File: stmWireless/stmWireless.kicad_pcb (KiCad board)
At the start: 4 copper layers, 49 parts, among them IC1 BALFLB-WL-02D3, J1 SWD, J2 CORTEX_DEBUG, J3 Power, J5 i2c3 header, U1 STM32WLE5CBU6, U2 AP63203WU, U3 BGS12WN6E6327, Y1 Crystal_32MHz, Y2 Crystal_32.768kHz

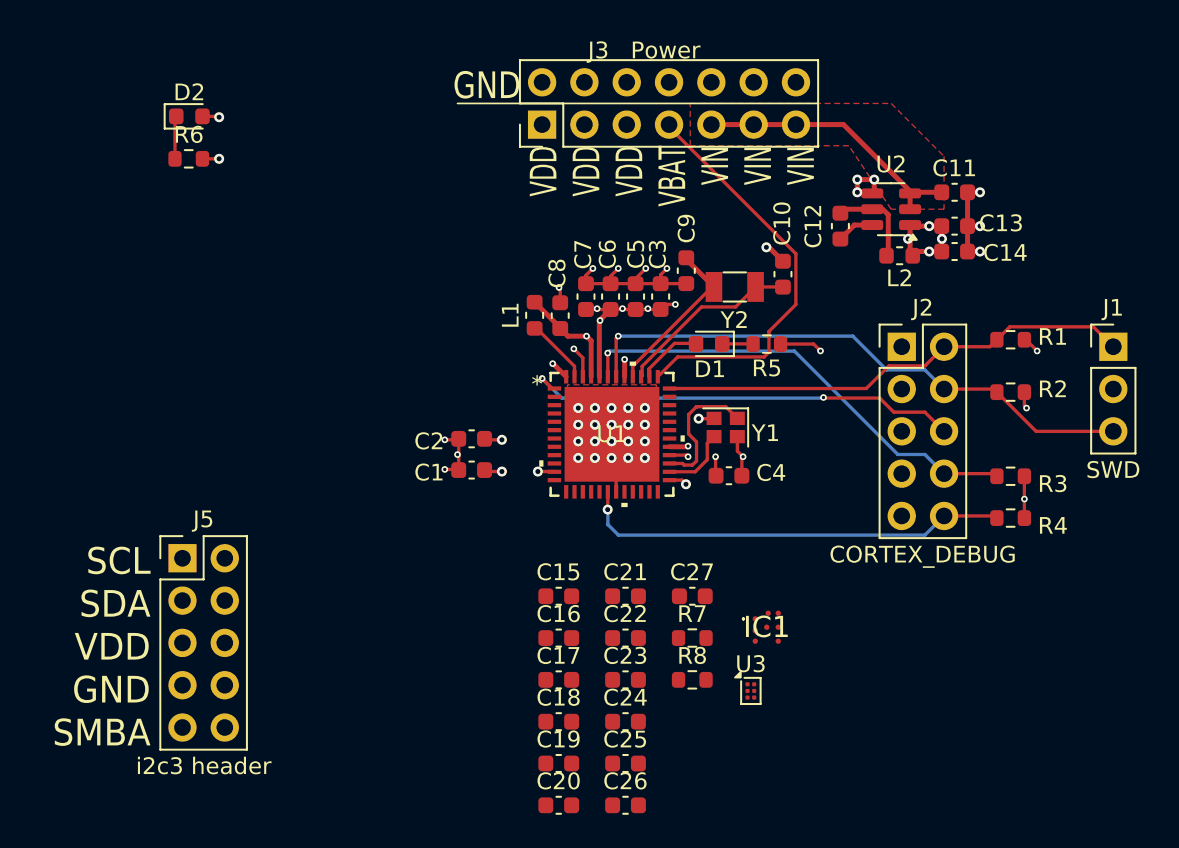
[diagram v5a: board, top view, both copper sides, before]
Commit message: add GPIO port of most unused pins
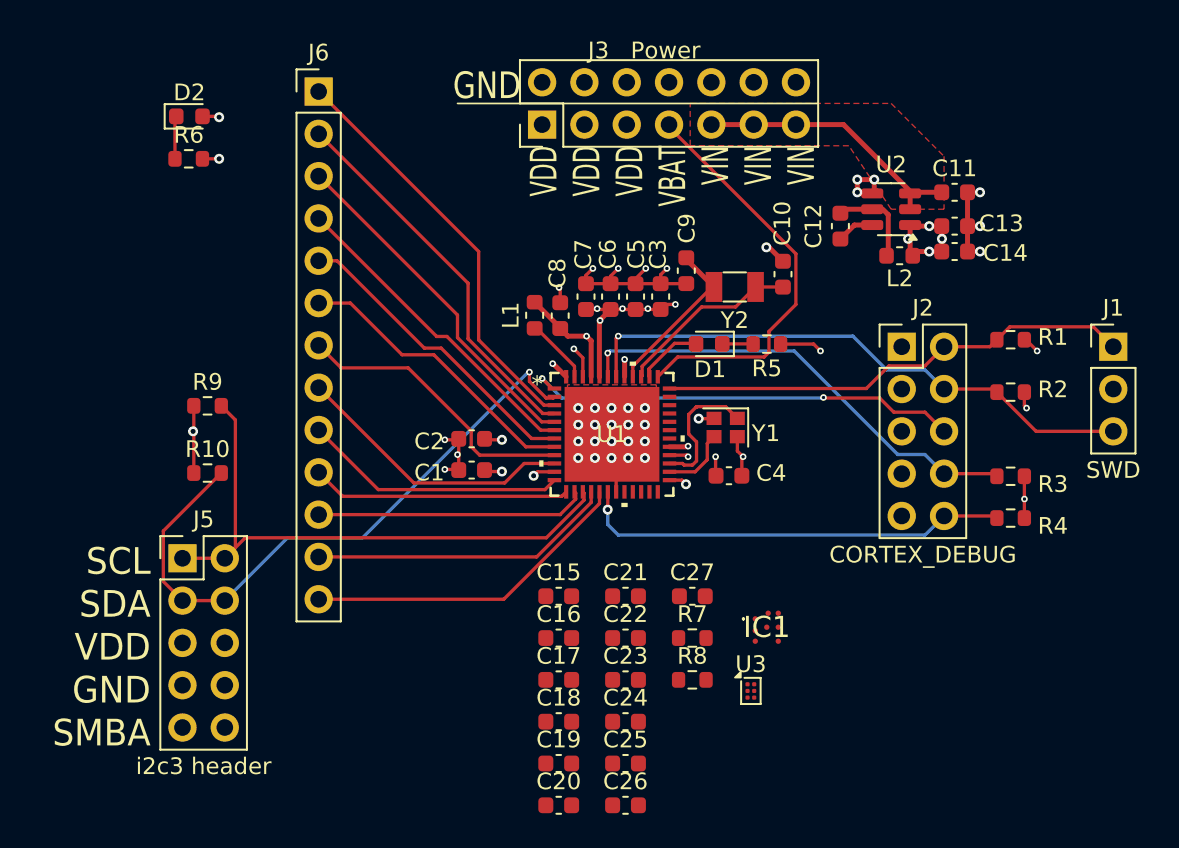
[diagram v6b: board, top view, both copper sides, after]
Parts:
- added J6: GPIO1, Connector_PinHeader_2.54mm:PinHeader_1x13_P2.54mm_Vertical, F.Cu at (122.5, 66.0)
- added R10: 4.k7, Resistor_SMD:R_0603_1608Metric, F.Cu at (115.8, 88.9)
- added R9: 4.7k, Resistor_SMD:R_0603_1608Metric, F.Cu at (115.8, 84.8)
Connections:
- U1 pad 10: unconnected-(U1-PA3-Pad10) -> Net-(J6-Pin_8)
- U1 pad 12: unconnected-(U1-PA4-Pad12) -> Net-(J6-Pin_9)
- U1 pad 13: unconnected-(U1-PA5-Pad13) -> Net-(J6-Pin_10)
- U1 pad 14: unconnected-(U1-PA6-Pad14) -> Net-(J6-Pin_11)
- U1 pad 16: unconnected-(U1-PA8-Pad16) -> Net-(J6-Pin_12)
- U1 pad 17: unconnected-(U1-PA9-Pad17) -> Net-(J6-Pin_13)
- U1 pad 3: unconnected-(U1-PB5-Pad3) -> Net-(J6-Pin_1)
- U1 pad 4: unconnected-(U1-PB6-Pad4) -> Net-(J6-Pin_2)
- U1 pad 5: unconnected-(U1-PB7-Pad5) -> Net-(J6-Pin_3)
- U1 pad 6: unconnected-(U1-PB8-Pad6) -> Net-(J6-Pin_4)
- U1 pad 7: unconnected-(U1-PA0-Pad7) -> Net-(J6-Pin_5)
- U1 pad 8: unconnected-(U1-PA1-Pad8) -> Net-(J6-Pin_6)
- U1 pad 9: unconnected-(U1-PA2-Pad9) -> Net-(J6-Pin_7)
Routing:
- net /i2c3_SDA: track 0.00 -> 38.6 mm, vias 0 -> 1
- net /i2c3_SCL: track 0.00 -> 35.8 mm
- net Net-(J6-Pin_1): track 0.00 -> 25.1 mm
- net Net-(J6-Pin_2): track 0.00 -> 23.1 mm
- net Net-(J6-Pin_3): track 0.00 -> 21.1 mm
- net Net-(J6-Pin_13): track 0.00 -> 19.9 mm
- net Net-(J6-Pin_4): track 0.00 -> 19.4 mm
- net Net-(J6-Pin_5): track 0.00 -> 18.6 mm
- net Net-(J6-Pin_12): track 0.00 -> 18.3 mm
- net Net-(J6-Pin_6): track 0.00 -> 17.7 mm
- net Net-(J6-Pin_7): track 0.00 -> 17.4 mm
- net Net-(J6-Pin_8): track 0.00 -> 17.0 mm
- net Net-(J6-Pin_11): track 0.00 -> 16.3 mm
- net Net-(J6-Pin_9): track 0.00 -> 15.9 mm
- net Net-(J6-Pin_10): track 0.00 -> 15.6 mm
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
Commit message: rotate crystal to shorten traces and clear space, and resolve many DRC issues
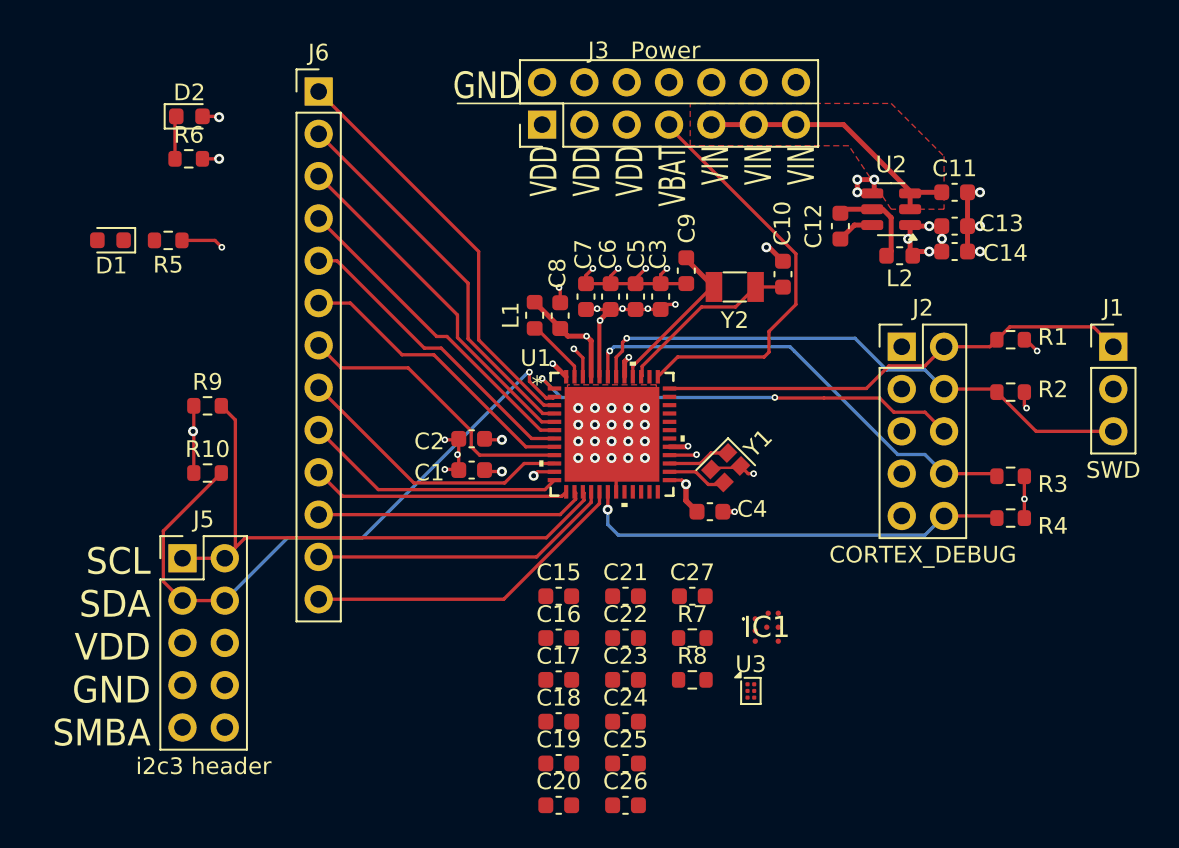
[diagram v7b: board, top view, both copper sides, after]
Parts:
- moved D1 36.5 mm to (110.0, 74.9)
- moved R5 36.5 mm to (113.4, 74.9)
- moved C4 2.44 mm to (146.0, 91.2)
- moved Y1 2.41 mm to (146.9, 88.5), turned to -135 degrees
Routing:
- net Net-(U1-OSC_OUT): track 8.15 -> 3.74 mm
- net (no net): track 3.60 -> 0.00 mm
- net Net-(D1-K): track 1.86 -> 0.00 mm
- net VDD: track 36.0 -> 37.1 mm, vias 21 -> 20
- net Net-(U2-SW): track 5.62 -> 6.57 mm
- net GND: track 38.0 -> 37.4 mm

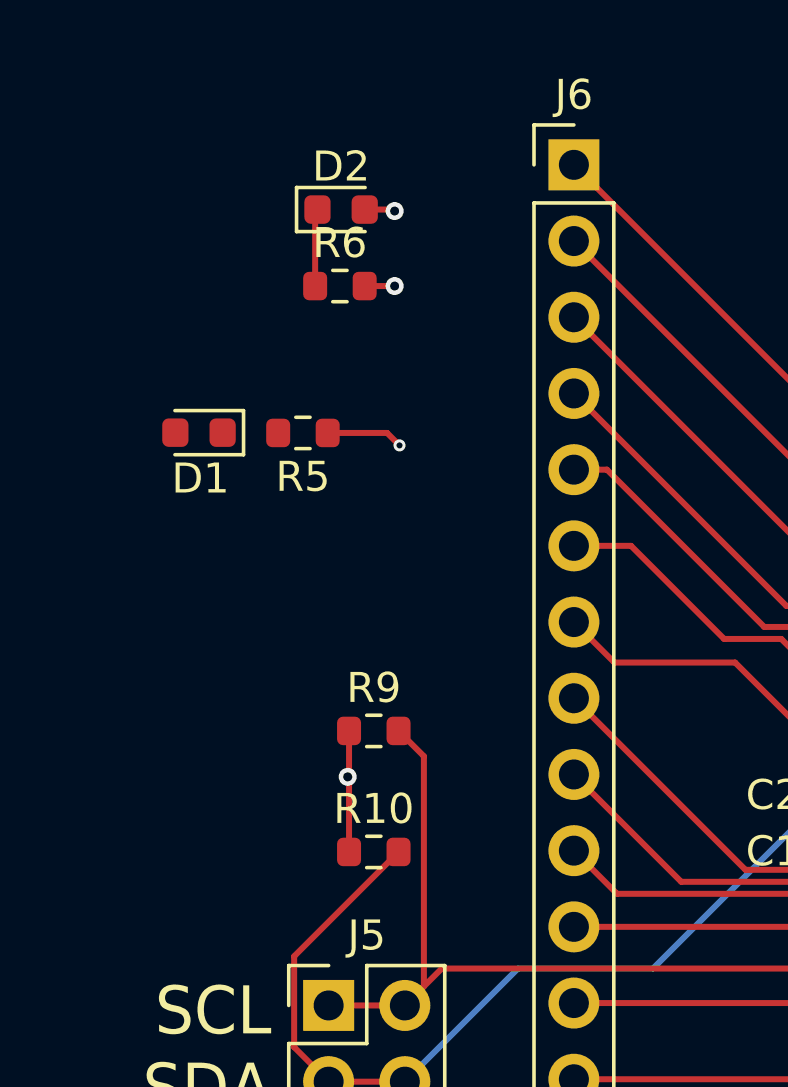
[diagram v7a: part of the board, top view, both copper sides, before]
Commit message: add start of GPIO pin labling (todo also lable features such as USARTRX/TX)
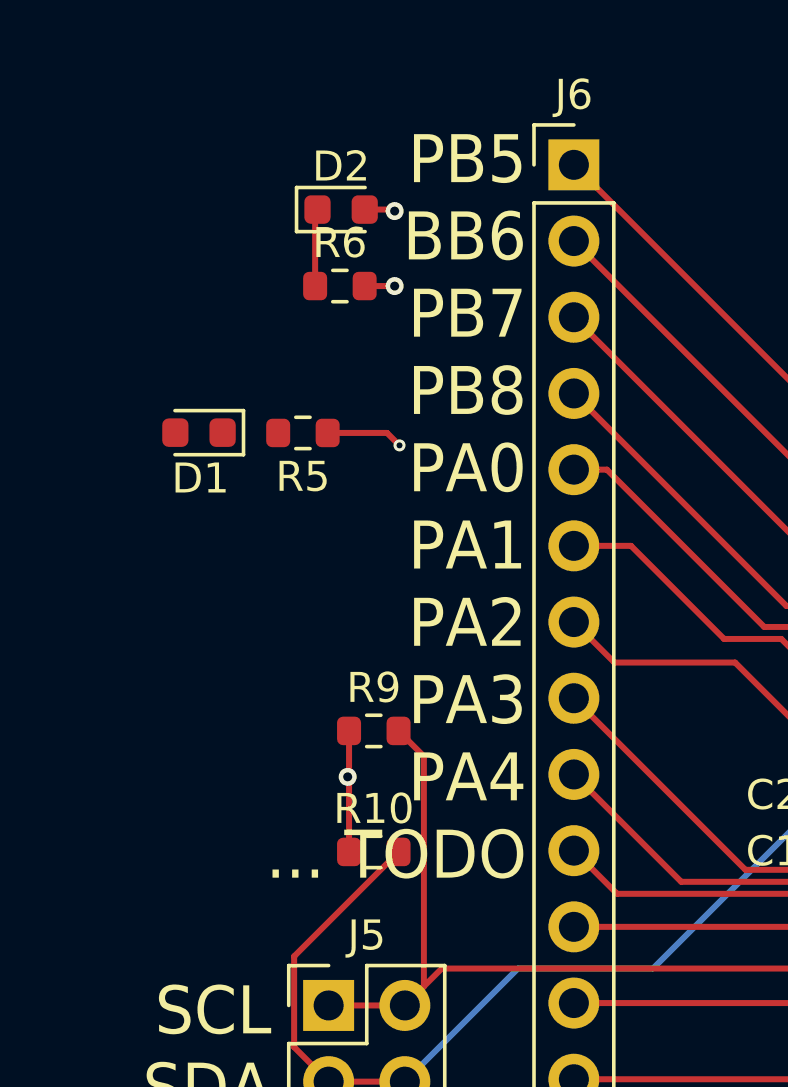
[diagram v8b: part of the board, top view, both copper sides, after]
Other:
- board text added: "PB5 BB6 PB7 PB8 PA0 PA1 PA2 PA3 PA4 ... TODO"
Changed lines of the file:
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@@
 		(layer "Cmts.User")
+	)
+	(gr_text "PB5\nBB6\nPB7\nPB8\nPA0\nPA1\nPA2\nPA3\nPA4\n... TODO"
+		(at 120.904 89.916 0)
+		(layer "F.SilkS")
+		(effects
+			(font
+				(size 1.6 1.5)
+				(thickness 0.1875)
+			)
+			(justify right bottom)
+		)
 	)
 	(gr_text "VDD\nVDD\nVDD\nVBAT\nVIN\nVIN\nVIN"
